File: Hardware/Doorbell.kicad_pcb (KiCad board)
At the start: 2 copper layers, 120 x 50 mm, 112 parts, among them J1 Conn_02x05_Odd_Even, J2 MEM2051-00-195-00-A, J3 1935174, Q1 SIA517DJ-T1-GE3, Q2 DMP4047LFDE-7, Q3 PMPB47XP, Q4 BC847, Q5 BC847, SW1 PEC12R-4115F-S0012, U1 CD4052BPWRG3, U10 AP1509-33SG-13, U11 PI4IOE5V9535LEX, U2 MAX98357AETE+T, U3 ATSAMG53N19B-AU, U4 VOS627A-X001T, U5 VOS627A-X001T, U6 MR25H128A, U7 LT6654BHS6-2.5-TRMPBF, U8 TLS4125D0EPV50XUMA1, U9 LM2903DR2G

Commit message: Clean up custom KiCad libraries
- Clean up the directory structure for KiCad custom libraries.
- Fix paths in KiCad schematic and pcb for symbols, footprints, and
3d models for custom libraries.
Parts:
- C29, C32: footprint Libs:EEH-AZK1E471B -> Capacitor_THT:EEH-AZK1E471B
- D4: value LTL-307P -> LED_Low_Batt; footprint Libs:Low_Batt_LED -> LED_THT:LTL-307P
- DS1: footprint Libs:C162BLBSBSW6WN33PAB -> Display:C162BLBSBSW6WN33PAB
- F1, F2: footprint Libs:FUSE_4527 -> Fuse:FUSE_4527
- J1: footprint Libs:3220-10-0100-00 -> Connector:3220-10-0100-00
- J2: footprint Libs:MEM2051-00-195-00-A -> Connector:MEM2051-00-195-00-A
- L1: footprint Libs:SRP1265C-220M -> Inductor_SMD:SRP1265C-220M
- L2: footprint Libs:CLF12577NIT-470M-D -> Inductor_SMD:CLF12577NIT-470M-D
- Q2: value DMP4047LFDE-7 -> TRANS_DMP4047LFDE-7; footprint Libs:DMP4047LFDE-7 -> Transistor_SMD:DMP4047LFDE-7
- Q3: footprint Libs:PMPB47XP -> Transistor_SMD:PMPB47XP
- R10, R9: footprint Libs:35501K3FT -> Resistor_SMD:35501K3FT
- RV2, RV5: footprint Libs:PTV09A-4015U-B103 -> Potentiometer:PTV09A-4015U-B103
- SW1: footprint Libs:PEC12R-4115F-S0012 -> Encoder:PEC12R-4115F-S0012
- U10: footprint Libs:AP1509-33SG-13 -> IC:AP1509-33SG-13
- U2: footprint Libs:MAX98357AETE_T -> IC:MAX98357AETE_T
- U3: footprint Libs:ATSAMG53N19B-AU -> IC:ATSAMG53N19B-AU
- U4, U5: footprint Libs:VOS627A-X001T -> IC:VOS627A-X001T
- U7: footprint Libs:LT6654BHS6-2.5-TRMPBF -> IC:LT6654BHS6-2.5-TRMPBF
- U8: footprint Libs:TLS4125D0EPV50XUMA1 -> IC:TLS4125D0EPV50XUMA1

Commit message: Switch to local libraries for KiCad schematic
- Move all KiCad schematic symbols into local libraries
- Fix KiCad schematic library links to point to local libraries
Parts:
- D4: value LED_Low_Batt -> LTL-307P
- J3: footprint TerminalBlock_Phoenix:TerminalBlock_Phoenix_PT-1,5-3-5.0-H_1x03_P5.00mm_Horizontal -> Connector:TerminalBlock_Phoenix_PT-1,5-3-5.0-H_1x03_P5.00mm_Horizontal
- Q2: value TRANS_DMP4047LFDE-7 -> DMP4047LFDE-7
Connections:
- RV2 pad 4: GND -> (no net)
- RV2 pad 5: GND -> (no net)
- RV5 pad 4: GND -> (no net)
- RV5 pad 5: GND -> (no net)

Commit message: Move KiCad global footprint and 3d models to local
- Move KiCad global footprint and 3d models to local directories
- Reassign footprints in KiCad schematic/PCB from global libraries to
  local libraries
- Reassign global 3d models to local 3d models for KiCad
- Update KiCad PCB with all local footprints
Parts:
- BT1, LS1: footprint Connector_Molex:Molex_MicroClasp_55935-0210_1x02_P2.00mm_Horizontal -> Connector:Molex_MicroClasp_55935-0210_1x02_P2.00mm_Horizontal
- D4: value LTL-307P -> LED_Low_Batt
- D6: footprint Diode_SMD:D_SMF -> Diode_SMD:V3FM12-M3_H
- J1: value Conn_02x05_Odd_Even -> 3220-10-0100-00
- Q1: footprint Package_TO_SOT_SMD:Vishay_PowerPAK_SC70-6L_Dual -> Transistor_SMD:Vishay_PowerPAK_SC70-6L_Dual
- Q2: value DMP4047LFDE-7 -> TRANS_DMP4047LFDE-7
- Q4, Q5: footprint Package_TO_SOT_SMD:SOT-23 -> Transistor_SMD:SOT-23
- U1: footprint Package_SO:TSSOP-16_4.4x5mm_P0.65mm -> IC:TSSOP-16_4.4x5mm_P0.65mm
- U11: footprint Package_SO:TSSOP-24_4.4x7.8mm_P0.65mm -> IC:TSSOP-24_4.4x7.8mm_P0.65mm
- U6: footprint Package_DFN_QFN:DFN-8-1EP_6x5mm_P1.27mm_EP2x2mm -> IC:DFN-8-1EP_6x5mm_P1.27mm_EP2x2mm
- U9: footprint Package_SO:SOIC-8_3.9x4.9mm_P1.27mm -> IC:SOIC-8_3.9x4.9mm_P1.27mm
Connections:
- RV2 pad 4: (no net) -> GND
- RV2 pad 5: (no net) -> GND
- RV5 pad 4: (no net) -> GND
- RV5 pad 5: (no net) -> GND
- U2 pad 12: (no net) -> unconnected-(U2-Pad12)
- U2 pad 13: (no net) -> unconnected-(U2-Pad13)
- U2 pad 5: (no net) -> unconnected-(U2-Pad5)
- U2 pad 6: (no net) -> unconnected-(U2-Pad6)

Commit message: Cleanup silkscreen
- Make sure component IDs are visible and clear
- Make sure pin 1 of IC's has marker
- Overall housekeeping of silkscreen layer
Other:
- board text added: "+"
- board text added: "6-30V DC"
- board text added: "8-34V AC"
- board text added: "Contrast"
- board text added: "Front"
- board text added: "Rear"
- board text added: "Trans"
- board text added: "Volume"

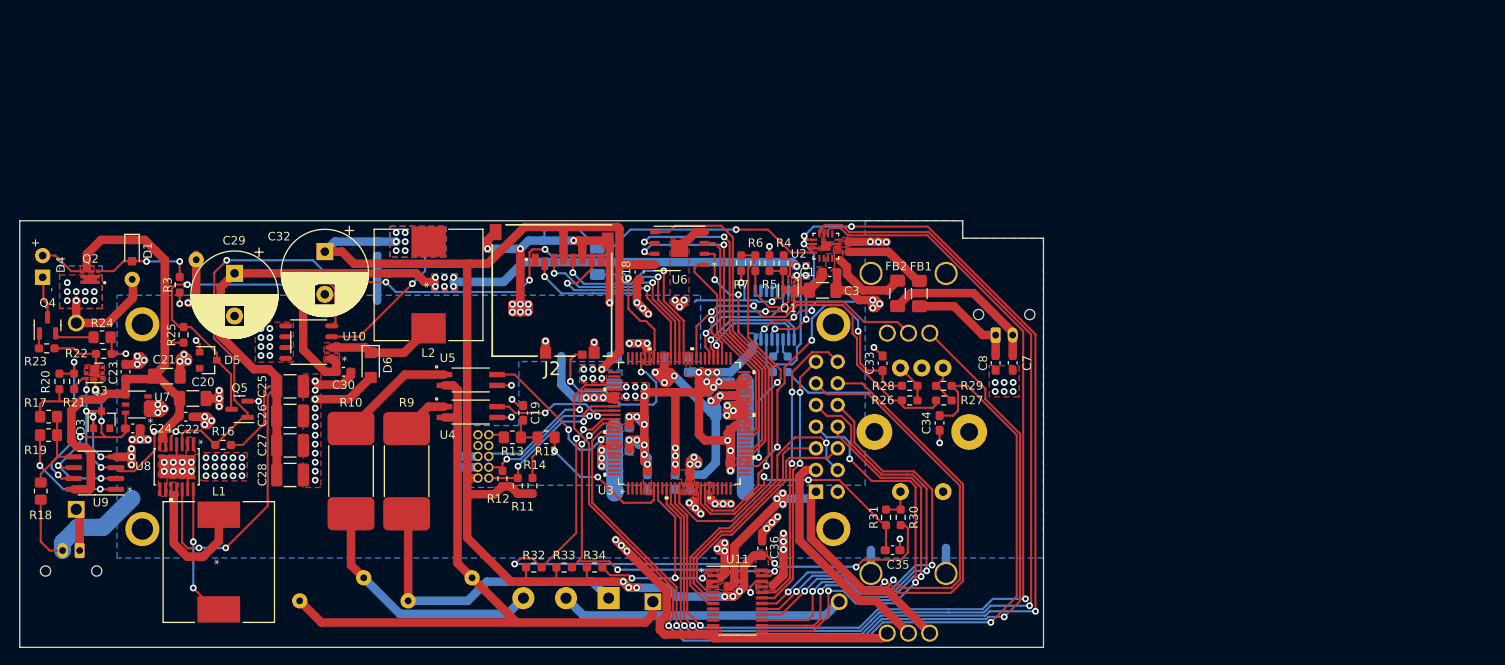
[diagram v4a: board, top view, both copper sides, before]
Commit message: Add some initial documentation and production files
- Add BOM to Docs in ods, pdf, and md formats
- Add Schematic to Docs in pdf format
- Add PCB layouts to Docs in pdf format
- Add 3D PCB images to Docs in png format
- Add 3D PCB VRML/wrl file to Docs
- Add component 3D models in step format to local libs in Hardware
  (needed to make KiCadStepUp happy)
- Add 3D PCB model to docs in step and fcstd formats
- Add gerbers and drill files to Production
- Add zip archive containing gerbers and drill files to Production
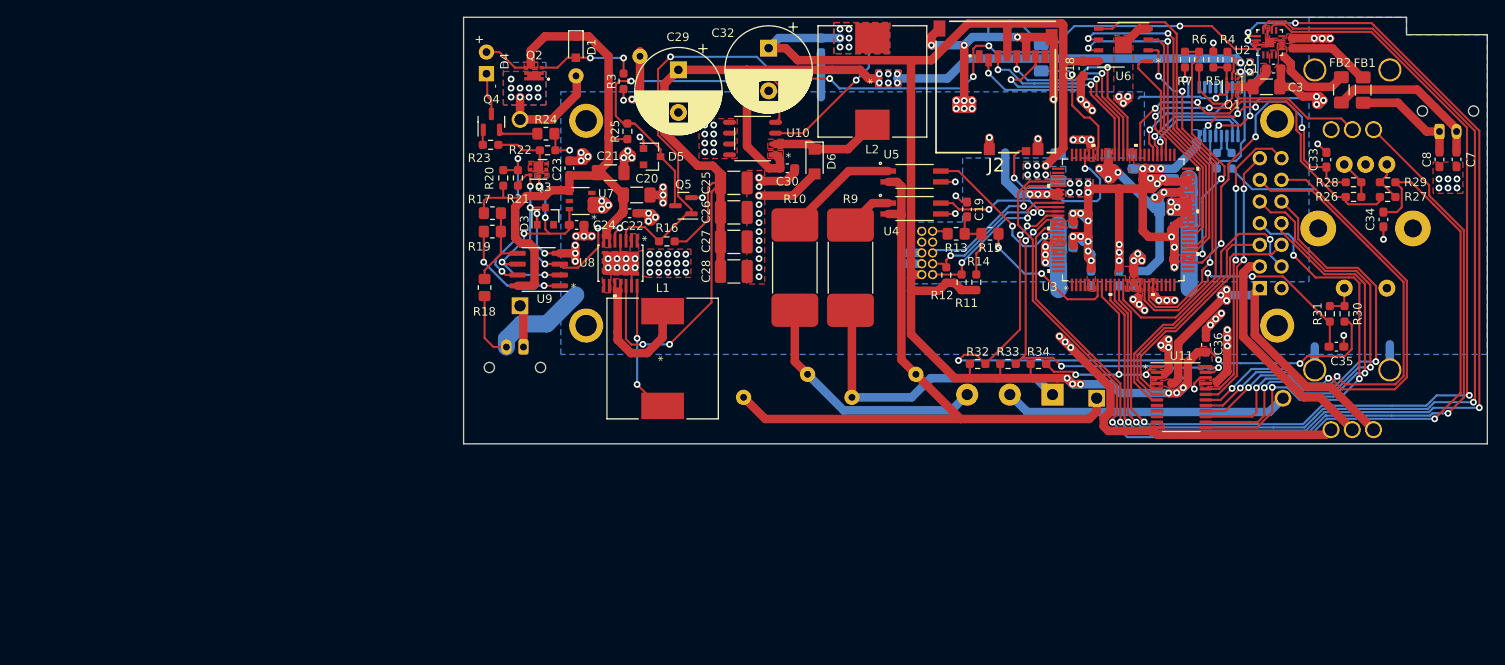
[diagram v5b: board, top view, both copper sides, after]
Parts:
- moved C1 57.2 mm to (185.0, 82.2)
- moved C10 57.2 mm to (166.9, 106.8)
- moved C15 57.2 mm to (159.7, 93.7)
- moved C33 57.2 mm to (191.2, 92.8)
- moved C34 57.2 mm to (197.8, 99.8)
- moved C5 57.2 mm to (168.6, 106.8)
- moved C6 57.2 mm to (165.6, 93.0)
- moved C7 57.2 mm to (206.4, 92.8)
- moved C8 57.2 mm to (204.4, 92.8)
- moved C9 57.2 mm to (163.6, 106.8)
- moved D2 57.2 mm to (152.4, 76.9)
- moved F2 57.2 mm to (175.2, 120.8)
- moved FB1 57.2 mm to (195.5, 84.7)
- moved FB2 57.2 mm to (192.9, 84.7)
- moved LS1 57.2 mm to (204.4, 89.5)
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
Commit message: Bump to board revision B
- Redesign low battery circuit
	- Replace comparator with PMIC
	- Utilize LED Driver IC
	- Remove unneeded 2.5v voltage reference
- Reroute some signals onto wkup/external interrupt pins
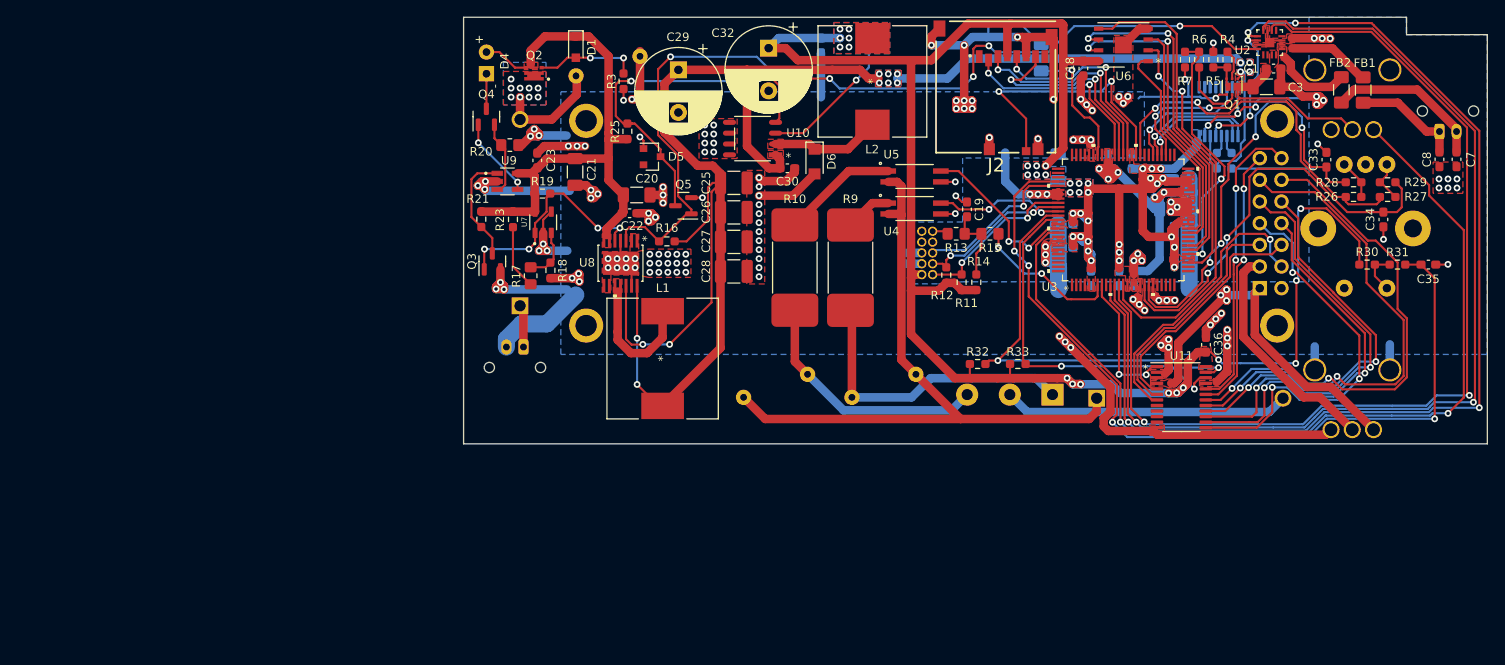
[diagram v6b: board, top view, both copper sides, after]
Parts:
- removed C24: 1u, Capacitor_SMD:C_0603_1608Metric_Pad1.08x0.95mm_HandSolder
- removed D3: BZX84-C8V2,235, Diode_SMD:D_SOT-23_ANK
- removed KiCad_Logo: KiCad-Logo2_5mm_SilkScreen, Symbol:KiCad-Logo2_5mm_SilkScreen
- removed OSHW_Logo: OSHW-Logo_7.5x8mm_SilkScreen, Symbol:OSHW-Logo_7.5x8mm_SilkScreen
- removed the R21 at (96.4, 95.0)
- removed R24: 180R, Resistor_SMD:R_0805_2012Metric_Pad1.20x1.40mm_HandSolder
- removed R34: 10k, Resistor_SMD:R_0603_1608Metric_Pad0.98x0.95mm_HandSolder
- D4: value LED_Low_Batt -> LTL-307P
- Q2: value TRANS_DMP4047LFDE-7 -> DMP4047LFDE-7
- Q3: value PMPB47XP -> BC847; footprint Transistor_SMD:PMPB47XP -> Transistor_SMD:SOT-23
- R17: value 1.8M -> 1M8
- R18: value 1.3M -> 1M; footprint Resistor_SMD:R_0805_2012Metric_Pad1.20x1.40mm_HandSolder -> Resistor_SMD:R_0603_1608Metric_Pad0.98x0.95mm_HandSolder
- R19: value 10M -> 1M; footprint Resistor_SMD:R_0805_2012Metric_Pad1.20x1.40mm_HandSolder -> Resistor_SMD:R_0603_1608Metric_Pad0.98x0.95mm_HandSolder
- R20: value 1M -> 15R; footprint Resistor_SMD:R_0603_1608Metric_Pad0.98x0.95mm_HandSolder -> Resistor_SMD:R_0805_2012Metric_Pad1.20x1.40mm_HandSolder
- R23: value 2k2 -> 2M2
- U7: value LT6654BHS6-2.5-TRMPBF -> MAX6457UKD3A+T; footprint IC:LT6654BHS6-2.5-TRMPBF -> IC:MAX6457UKD3A+T
- U9: value LM2903DR2G -> AL5816W5-7; footprint IC:SOIC-8_3.9x4.9mm_P1.27mm -> IC:AL5816W5-7
- moved C35 14.4 mm to (203.1, 105.1)
- moved Q3 12.1 mm to (93.4, 104.8), turned to 90 degrees
- moved R21 11.2 mm to (92.1, 99.8), turned to -90 degrees
- moved U9 11.0 mm to (95.2, 95.4), turned to 0 degrees
- moved R31 9.81 mm to (199.5, 105.1), turned to 180 degrees
- moved R23 9.13 mm to (95.8, 99.8), turned to -90 degrees
- moved R17 8.60 mm to (97.9, 106.4), turned to 90 degrees
- moved R18 7.98 mm to (100.2, 105.8)
- moved R19 7.37 mm to (99.3, 96.8)
- moved R30 6.35 mm to (195.9, 105.1), turned to 0 degrees
- moved U7 5.05 mm to (99.4, 100.2), turned to 90 degrees
- moved C21 4.17 mm to (103.1, 94.3), turned to -90 degrees
- moved R20 3.93 mm to (95.4, 91.1), turned to 0 degrees
- moved C23 3.87 mm to (98.7, 92.9)
- moved R33 1.15 mm to (155.0, 116.8)
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- renumbered R22 to R21
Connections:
- Q3 pad 2: Net-(D3-Pad1) -> GND
- Q3 pad 3: +2V5 -> Net-(Q3-Pad3)
- R17 pad 1: /Power/VBAT -> Net-(R17-Pad1)
- R19 pad 1: Net-(R19-Pad1) -> /Power/VBAT
- R19 pad 2: Net-(R17-Pad2) -> Net-(Q3-Pad1)
- R20 pad 1: /Power/VBAT -> Net-(Q4-Pad2)
- R20 pad 2: Net-(R20-Pad2) -> GND
- R21 pad 1: Net-(Q3-Pad1) -> /Power/VBAT
- R21 pad 2: GND -> Net-(Q3-Pad3)
- R23 pad 1: Net-(Q4-Pad1) -> /Power/VBAT
- R23 pad 2: Net-(Q3-Pad1) -> Net-(R17-Pad1)
- RV2 pad 1: Net-(RV2-Pad1) -> POT_PWR
- SW1 pad 1: Net-(R30-Pad2) -> GND
- SW1 pad 2: GND -> Net-(R30-Pad2)
- U3 pad 18: ENC_SW -> ENC_B
- U3 pad 60: unconnected-(U3-Pad60) -> ~{Card_Detect}
- U3 pad 72: ~{Card_Detect} -> unconnected-(U3-Pad72)
- U3 pad 79: ENC_B -> ENC_SW
- U3 pad 90: Net-(RV2-Pad1) -> Rear
- U3 pad 91: Rear -> POT_PWR
- U7 pad 1: GND -> Net-(Q3-Pad1)
- U7 pad 3: unconnected-(U7-Pad3) -> Net-(R17-Pad2)
- U7 pad 4: /Power/VBAT -> GND
- U7 pad 5: unconnected-(U7-Pad5) -> /Power/VBAT
- U8 pad 5: Net-(D3-Pad1) -> Net-(Q3-Pad1)
- U9 pad 1: Net-(R19-Pad1) -> Net-(Q3-Pad3)
- U9 pad 2: +2V5 -> GND
- U9 pad 3: Net-(D3-Pad1) -> Net-(Q4-Pad2)
- U9 pad 4: GND -> Net-(Q4-Pad1)
- U9 pad 5: Net-(R17-Pad2) -> /Power/VBAT
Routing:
- net Net-(RV2-Pad1): track 107.2 -> 0.00 mm, vias 2 -> 0
- net POT_PWR: track 0.00 -> 106.4 mm, vias 0 -> 2
- net ENC_B: track 115.4 -> 49.2 mm
- net ENC_SW: track 31.7 -> 97.5 mm, vias 2 -> 4
- net GND: track 362.3 -> 392.9 mm, vias 144 -> 147
- net Net-(D3-Pad1): track 29.1 -> 0.00 mm, vias 5 -> 0
- net +2V5: track 28.9 -> 0.00 mm, vias 5 -> 0
- net Net-(R20-Pad2): track 19.7 -> 0.00 mm, vias 2 -> 0
- net Net-(Q3-Pad1): track 7.16 -> 26.7 mm, vias 0 -> 4
- net +5V: track 190.7 -> 209.3 mm
- net +3V3: track 306.7 -> 323.4 mm, vias 47 -> 49
- net Net-(R19-Pad1): track 13.6 -> 0.00 mm, vias 2 -> 0
- net Net-(Q3-Pad3): track 0.00 -> 13.0 mm
- net /Power/VBAT: track 76.9 -> 65.0 mm
- net ~{Card_Detect}: track 21.7 -> 31.8 mm
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- removed copper zone on F.Cu, net +2V5
- removed copper zone on F.Cu, net Net-(Q3-Pad1)
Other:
- board text added: "6-28V DC"
- board text removed: "6-30V DC"
